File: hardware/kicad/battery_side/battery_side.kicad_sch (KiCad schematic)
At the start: 41 parts, among them J1 Conn_01x02, J2 RJ45, J3 USB-OTG, J5 UART-DBG, Q1 AO3401A, Q2 AO3400A, U1 TPS62933FDRLR, U2 R-78E12-1.0, U3 SN65HVD3082E

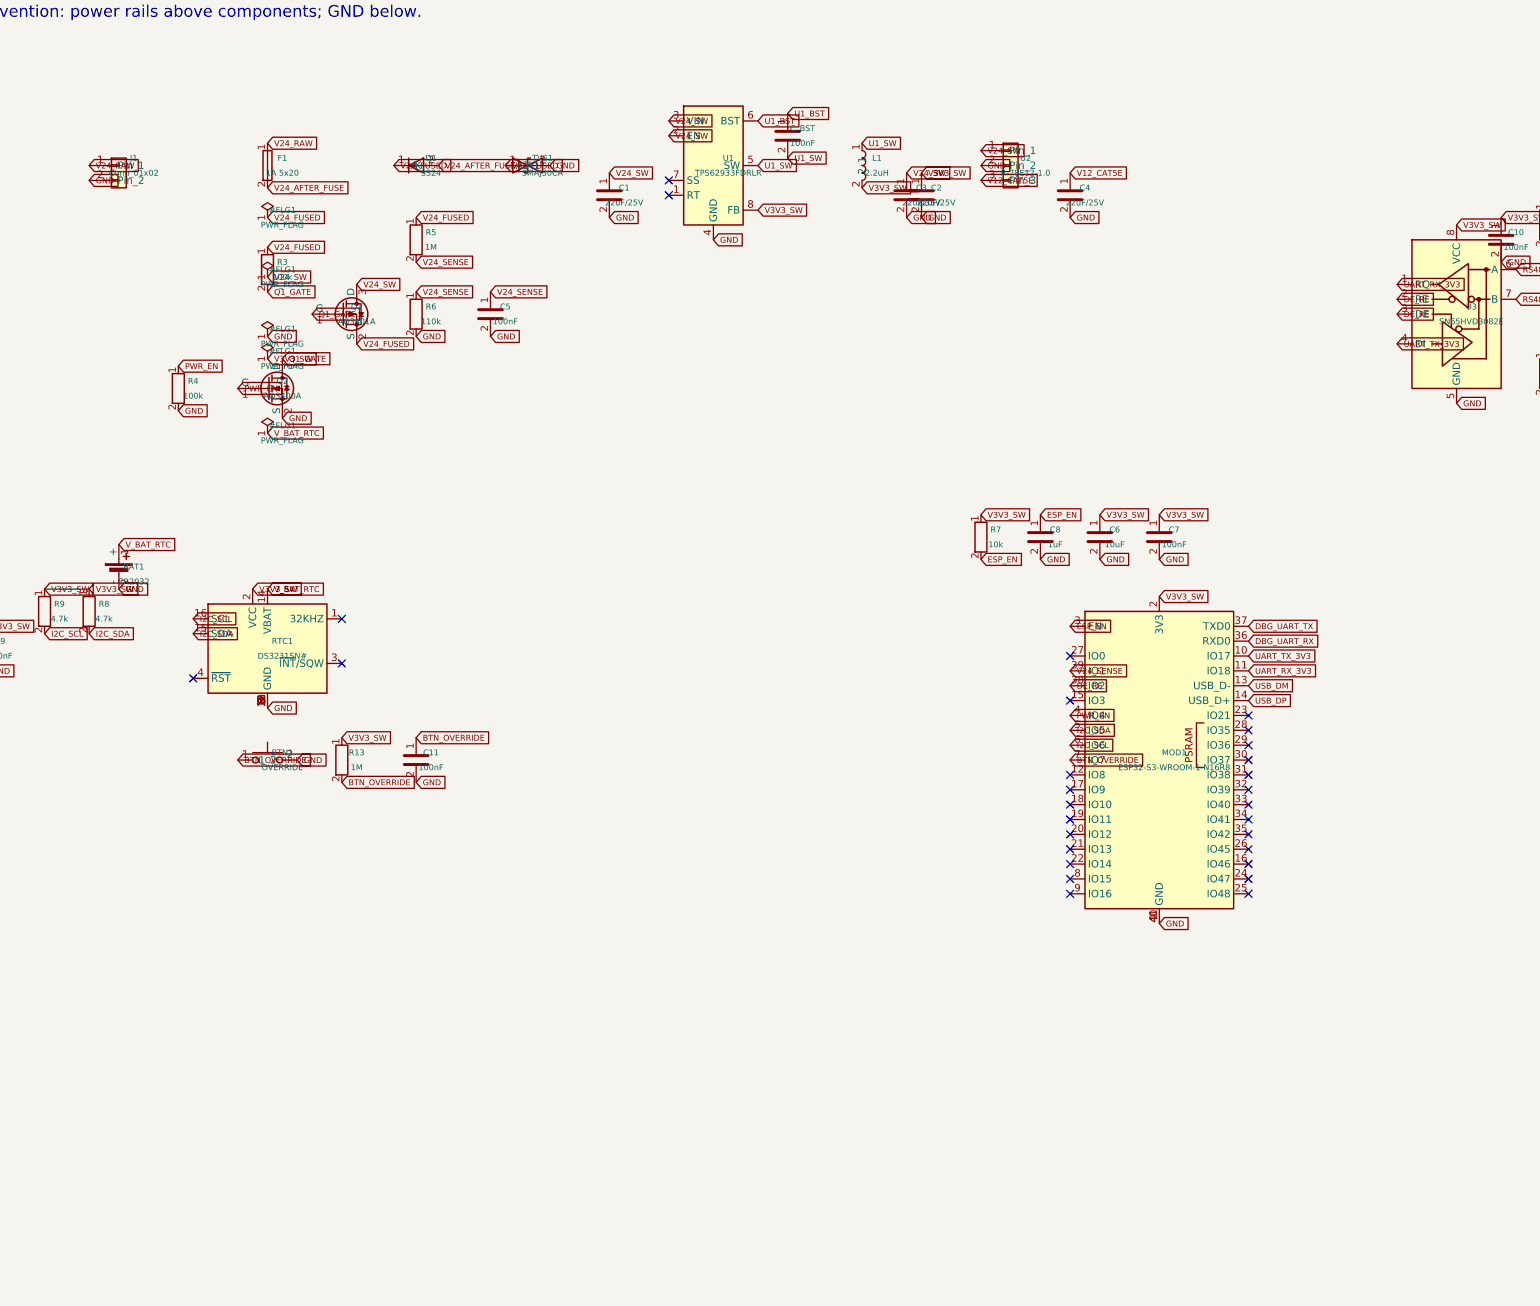
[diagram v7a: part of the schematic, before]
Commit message: hardware: CP-schematic-cleanup iter 20 — Finding 06 (V24_* label cluster) fix
Two root-cause fixes for the upper-left D1/TVS1/Q1 dense cluster:

1. Power-input row spread across A3 width
   F1:   60*G -> 65*G  (+6.35 mm)
   D1:   80*G -> 95*G  (+19.05 mm)
   TVS1: 95*G -> 120*G (+31.75 mm)
   U1:   120*G -> 155*G (+44.45 mm)
   U2:   160*G -> 200*G (+50.8 mm)

   Each component now has 25-50mm horizontal gap from its
   neighbors, giving the V24_FUSED / V24_AFTER_FUSE labels
   (~7-15mm wide) clear breathing room.

2. PWR_FLAG column relocated to bottom strip
   The 5 PWR_FLAGs (V24_FUSED, GND, V24_SW, V3V3_SW, V_BAT_RTC)
   used to anchor at x=R5_X-20*G=60*G — exactly F1's column —
   producing the V24_* horizontal stack Codex flagged.

   Moved to a dedicated horizontal strip at y=180*G=228.6mm
   (lower half of A3 sheet, well below all other components),
   spaced 20*G=25.4mm apart in x. The lower half of the page is
   finally used.

Children of U1 (L1, C1, C2, C_BST) and U2 (C3, C4) follow their
parent's X derivation automatically. Sense divider + hard-cut
unchanged this iter.

ERC 0/0 on both. PCB DRC 0 errors. Netlist topology preserved
(only position metadata changed).

CODEX: visual re-check needed. Confirm D1/TVS1/Q1 V24_* cluster
resolved; flag any new offender with coords.

Co-Authored-By: Claude Opus 4.7 (1M context) <noreply@anthropic.com>
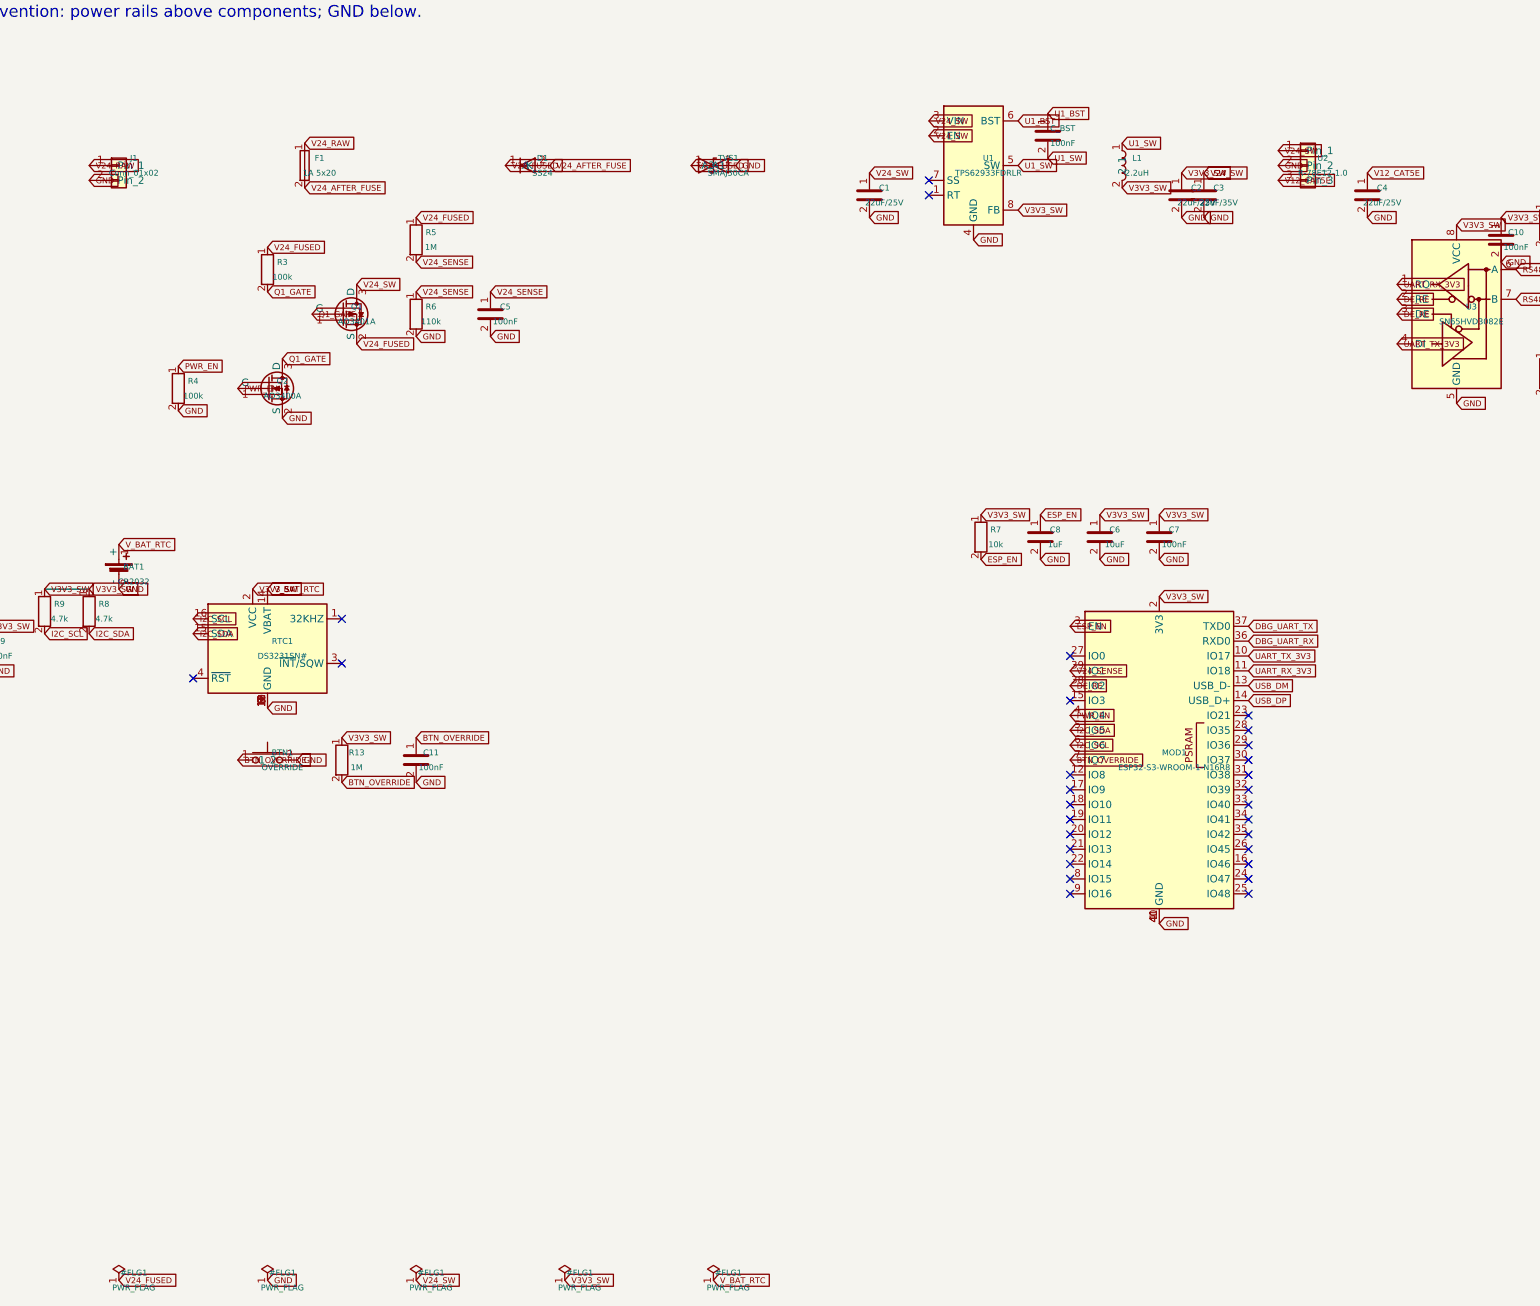
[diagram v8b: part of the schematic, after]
